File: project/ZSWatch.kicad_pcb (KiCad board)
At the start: 4 copper layers, 41 x 38 mm, 94 parts, among them IC101 nPM1300-QEXX, IC201 APDS-9306-065, IC202 BMI270, IC203 BMP581, IC204 LIS2MDLTR, IC205 BME688, IC301 ESDALC6V1W5, IC302 FAN5622SX, IC303 MX25U51245GZ4I00, IC304 TS3USB221A, IC305 NTS0104GU12, IC306 DRV2603RUNT, IC307 RV-8263-C8, M301 NORA-B106, Q201 DMG1013UW-7, Q301 BC817W, Q302 PMZ550UNEYL, Q303 PMZ550UNEYL, X101 BATTERY, X301 DOCK, X302 GC9A01A_CST816S, X303 M+, X304 M-

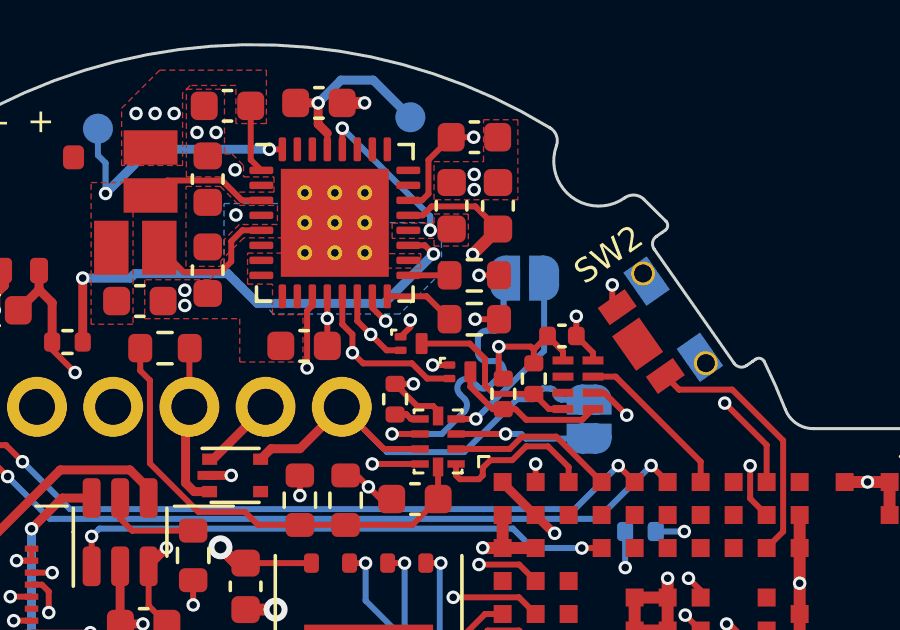
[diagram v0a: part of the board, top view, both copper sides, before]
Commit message: Change layer for PCB tables to User1
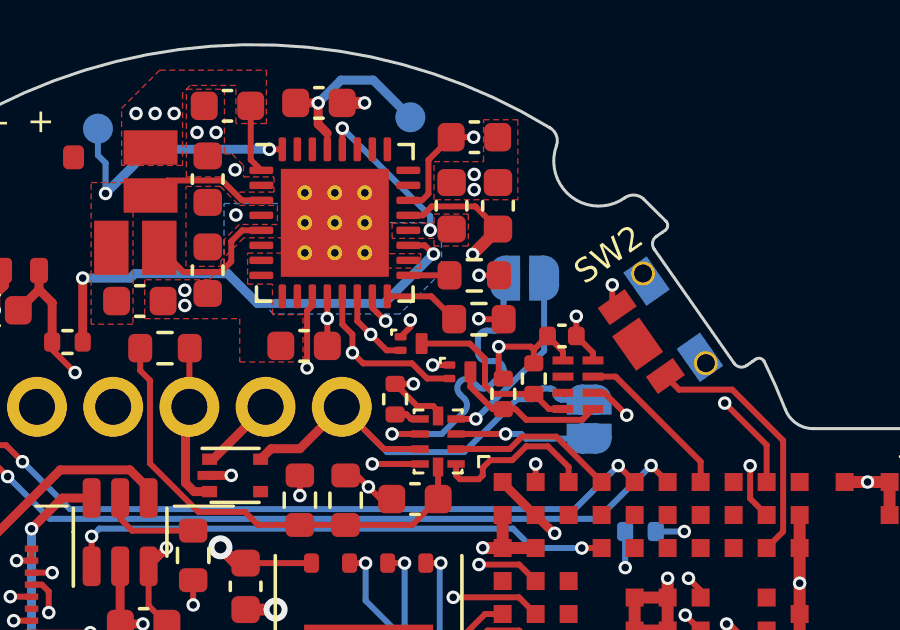
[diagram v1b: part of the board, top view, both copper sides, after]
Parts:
- moved R102 0.16 mm to (166.9, 102.9)
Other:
- board text added: "0,9820 mm"
- board text added: "40,9576 mm x 37,9989 mm"
- board text added: "Dielektrikum"
- board text added: "Tangens des Verlustwinkels"
- board text removed: "0,9800 mm"
- board text removed: "40,9601 mm x 37,9900 mm"
- board text removed: "Dielektrikum 1"
- board text removed: "Dielektrikum 2"
- board text removed: "Dielektrikum 3"
- board text removed: "Verlustfaktor"
